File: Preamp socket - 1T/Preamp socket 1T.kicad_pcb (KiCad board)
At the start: 2 copper layers, 23 x 17.8 mm, 12 parts, among them J1 In, J2 VCC, J3 Out, J4 GND, U1 Preamp

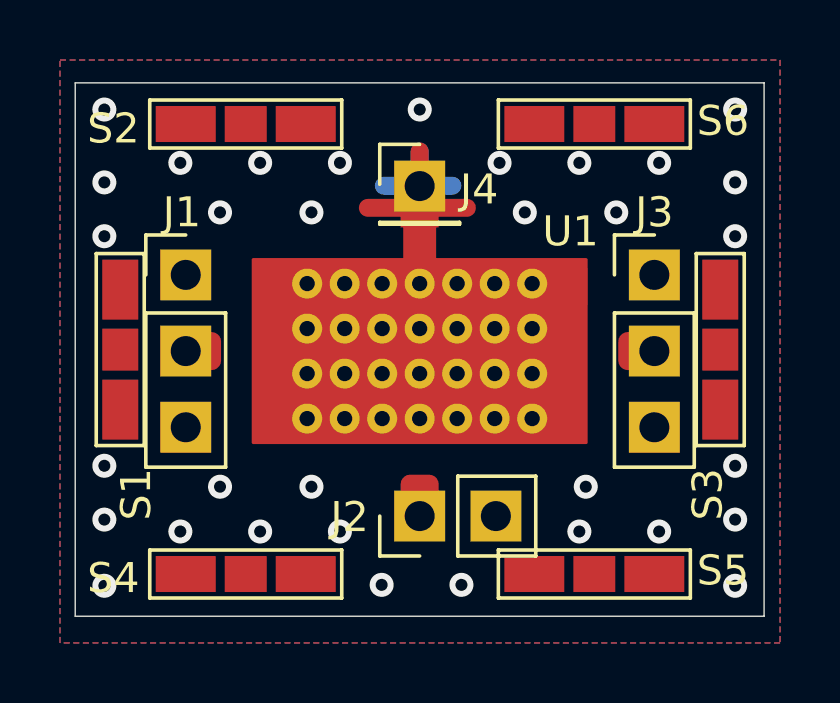
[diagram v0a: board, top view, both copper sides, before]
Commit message: Added: 1T preamp socket. 3D renders.
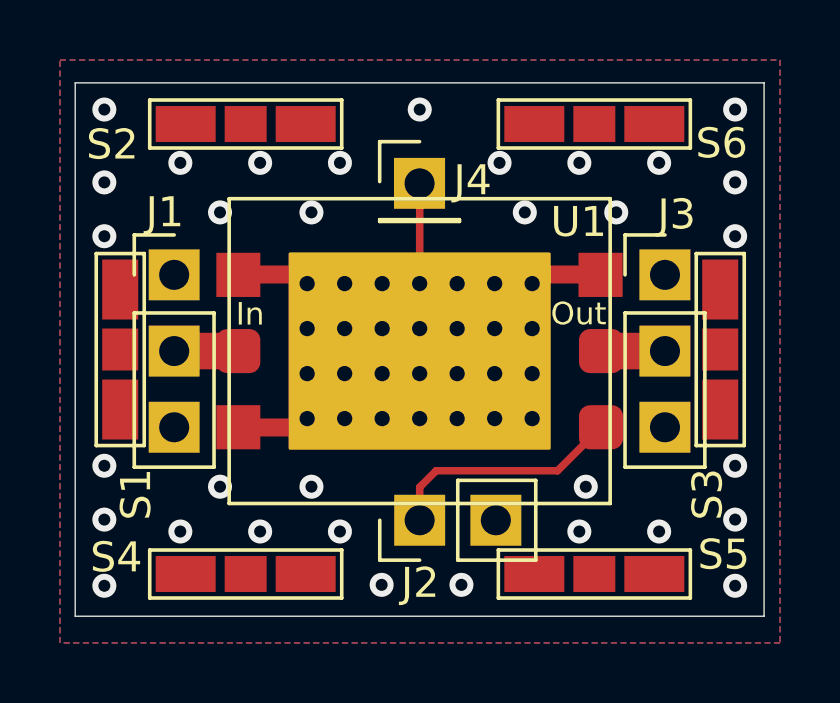
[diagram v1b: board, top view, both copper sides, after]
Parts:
- U1: footprint _Custom_footprints:Preamp_WMA7RA-R5 -> _Custom:Preamp_WMA1R0C
- moved J1 0.39 mm to (148.8, 96.6)
- moved J3 0.35 mm to (165.2, 96.6)
- moved J2 0.14 mm to (157.0, 104.8)
- moved J4 0.09 mm to (157.0, 93.5)
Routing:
- net GND: track 11.5 -> 2.50 mm
- net Net-(J2-Pad1): track 0.00 -> 7.97 mm
- net Net-(J1-Pad2): track 0.00 -> 3.01 mm
- net Net-(J3-Pad2): track 0.00 -> 3.01 mm
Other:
- board text added: "In"
- board text added: "Out"
- board text added: "Preamp socket 1T"
- board text removed: "Preamp socket"

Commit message: Updated 3D settings
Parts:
- added REF**: Shield_15mm_20mm, _Custom:Shield_15mm_20mm, F.Cu at (157.1, 99.0)
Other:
- board text added: "03/2020 v0.2"
- board text removed: "02/2020 v0.1"

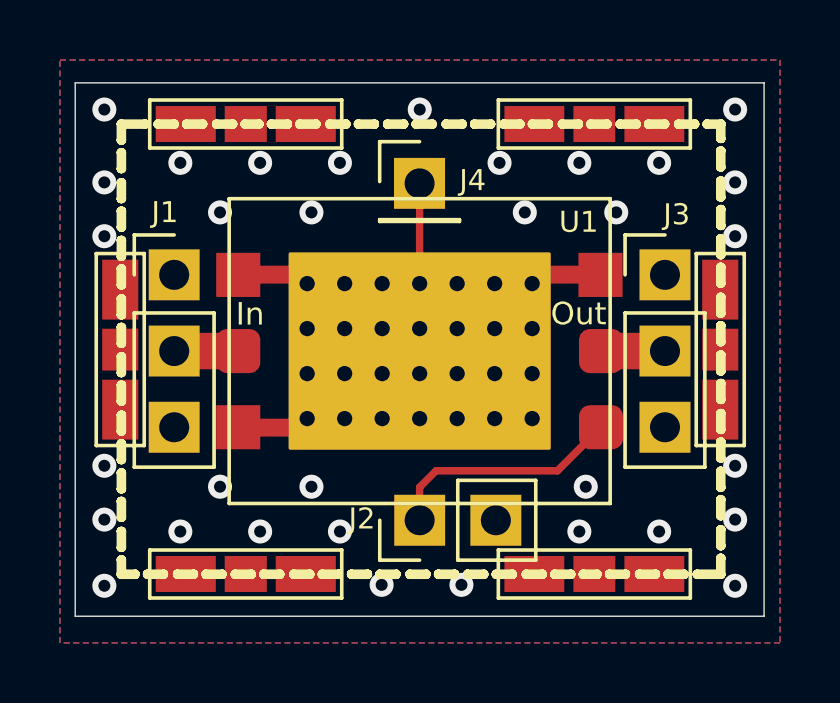
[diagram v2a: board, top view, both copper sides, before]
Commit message: Changed: header hole size, header to preci-dip header
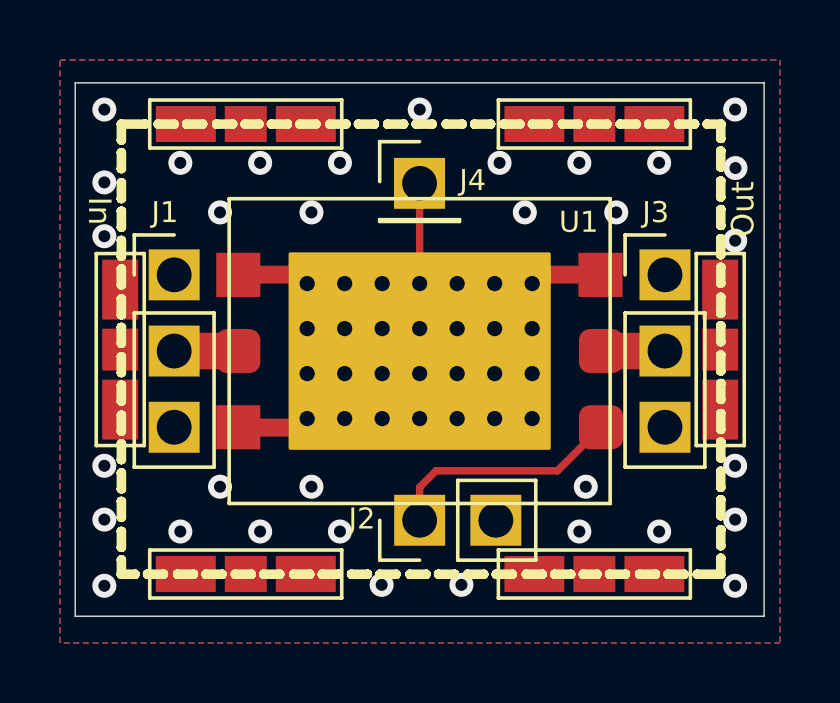
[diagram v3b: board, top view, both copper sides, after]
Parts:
- J1, J3: footprint _Custom_footprints:PinHeader_1x03_P2.54mm_Vertical_rectangular -> _Custom:Preci-dip_PinHeader_1x03_rect
- J2: footprint Connector_PinHeader_2.54mm:PinHeader_1x02_P2.54mm_Vertical -> _Custom:Preci-dip_PinHeader_1x02_rect
- J4: footprint Connector_PinHeader_2.54mm:PinHeader_1x01_P2.54mm_Vertical -> _Custom:Preci-dip_PinHeader_1x01_rect
- moved G1 0.45 mm to (163.8, 93.1)
